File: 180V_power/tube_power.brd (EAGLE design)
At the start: 55 x 30 mm, 28 parts, among them IC1 NE555D, Q1 IRF740S, U1 TLV1117-5SOT-223, U2 2N7002

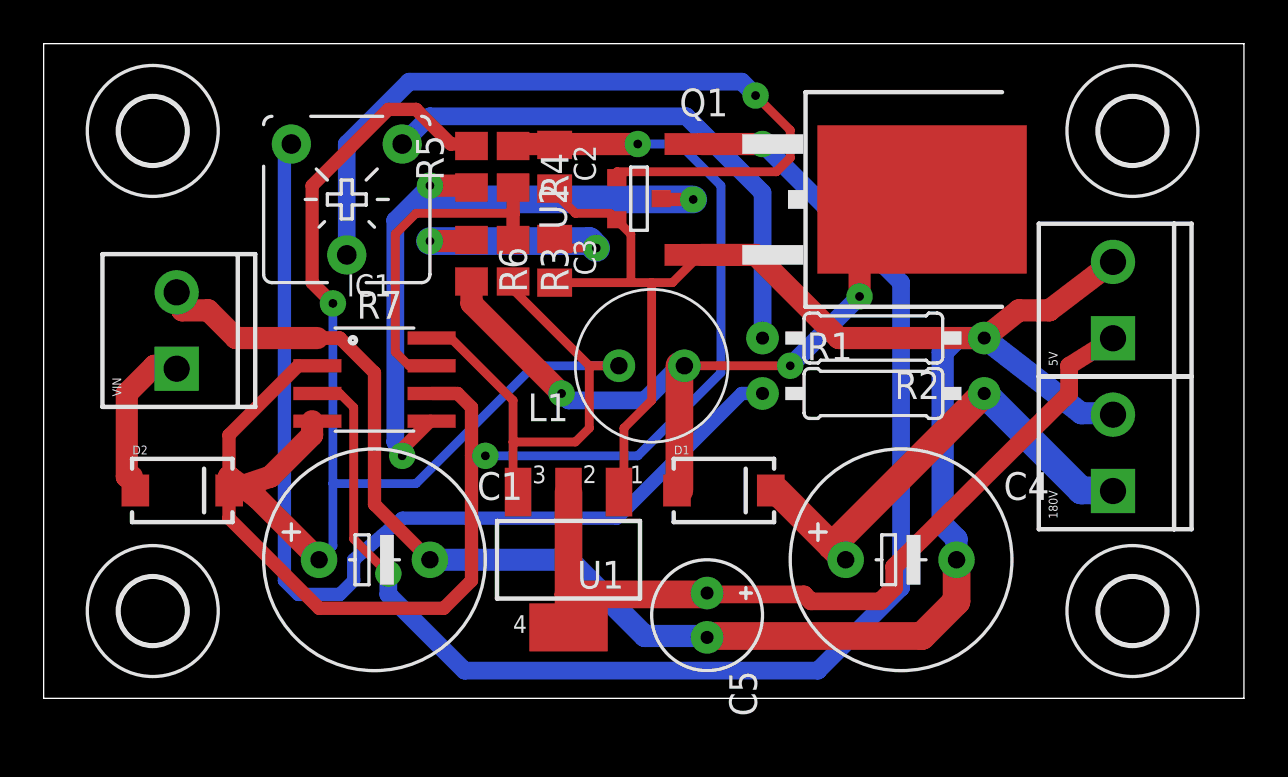
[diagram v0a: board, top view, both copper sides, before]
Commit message: new 180V board design
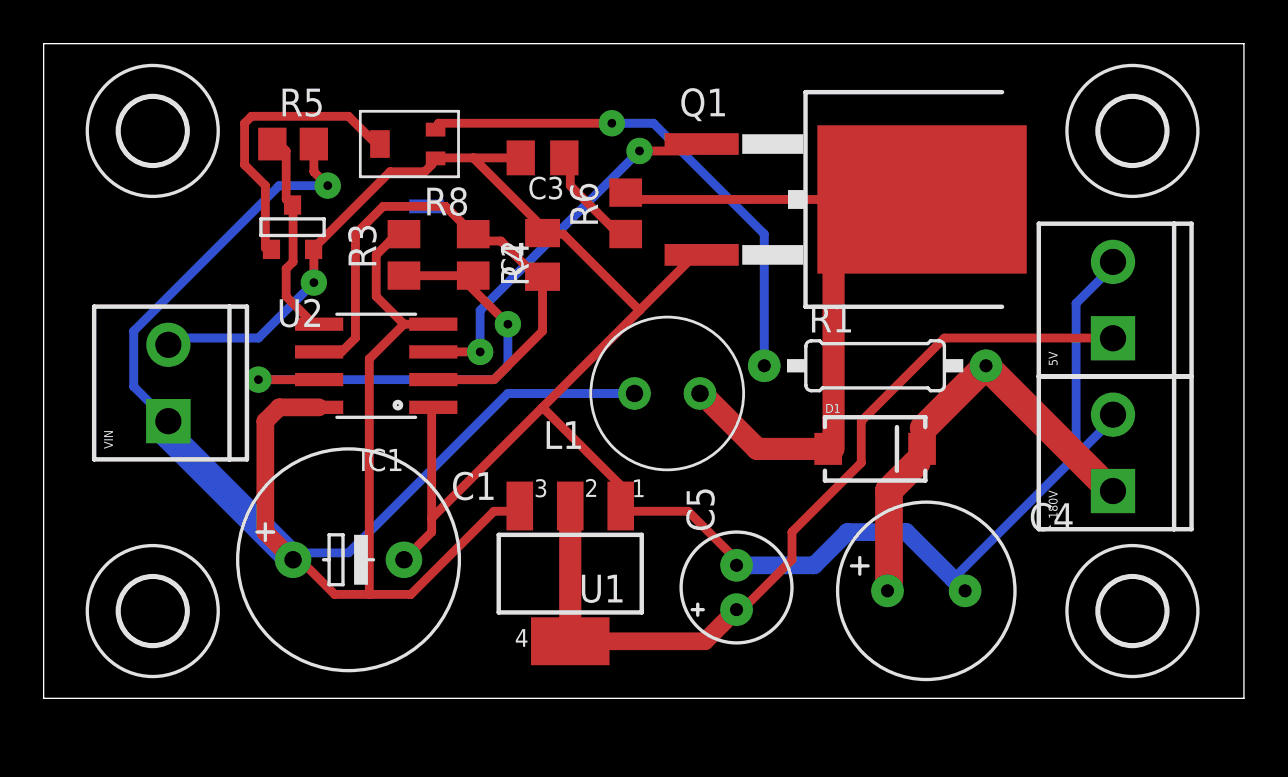
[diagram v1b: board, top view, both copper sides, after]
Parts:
- removed D2: (no value), iStivi - RCLD:SMA-DIODE
- removed R2: 470R, iStivi - RCLD:0207/10
- removed R7: 1K, iStivi - RCLD:CA6V
- added R8: (no value), iStivi - RCLD:TRIM-EVM2N
- C4: device iStivi - RCLD:E5-10,5 -> iStivi - RCLD:E3,5-8
- moved U2 15.9 mm to (11.4, 21.6), turned to 180 degrees
- moved R5 8.24 mm to (11.4, 25.4), turned to 0 degrees
- moved R6 7.39 mm to (26.7, 22.2), turned to 90 degrees
- moved D1 7.19 mm to (38.1, 11.4)
- moved R3 5.01 mm to (16.5, 20.3), turned to 90 degrees
- moved C3 4.75 mm to (22.9, 24.8), turned to 180 degrees
- moved R4 4.43 mm to (19.7, 20.3)
- moved C2 4.08 mm to (22.9, 20.3), turned to 90 degrees
- moved VIN 2.43 mm to (5.71, 12.7)
- moved C5 1.85 mm to (31.8, 5.08), turned to 90 degrees
- moved C4 1.83 mm to (40.4, 4.93)
- moved L1 1.46 mm to (28.6, 14.0)
- moved R1 1.27 mm to (38.1, 15.2)
- moved C1 1.19 mm to (14.0, 6.35)
- moved IC1 0.64 mm to (15.2, 15.2), turned to 90 degrees
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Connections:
- removed net R2: R2.2, R7.A
- removed net VAR: R7.S, U2.1
- net GND: now also R8.P$1; no longer R2.1
- net N$1: now also R8.P$2, U2.1; no longer D2.A, VIN.1
- net R1: now also R8.P$3; no longer R7.E
- net VCC: now also VIN.1; no longer D2.C
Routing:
- net OUT: track 63.4 -> 17.4 mm
- net THR: track 64.6 -> 25.8 mm, vias 2 -> 0
- net VAR: track 37.2 -> 0.00 mm, vias 1 -> 0
- net R2: track 25.2 -> 0.00 mm
- net R1: track 46.6 -> 23.4 mm, vias 0 -> 1
- net CON: track 31.2 -> 9.74 mm, vias 3 -> 0
- net GND: track 113.8 -> 101.4 mm, vias 0 -> 1
- net VCC: track 77.0 -> 88.4 mm
- net DIS: track 15.5 -> 23.3 mm, vias 0 -> 2
- net R6: track 11.8 -> 5.18 mm, vias 2 -> 0
- net N$1: track 7.57 -> 13.3 mm
- net 180V: track 22.5 -> 20.5 mm
- net L1: track 34.3 -> 32.5 mm, vias 3 -> 0
- net 5V: track 37.5 -> 38.7 mm
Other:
- board text added: "1"
- board text added: "2"
- board text added: "3"
- board text added: "4"
- board text added: "TUBE POWER SUPPLY"
- board text removed: "10uF"
- board text removed: "330uF"
- board text removed: "9-12V"
- board text removed: "C4"
- board text removed: "IRF740"
- board text removed: "L1"
- board text removed: "NIXIE POWER SUPPLY"
- board text removed: "R1"
- board text removed: "R2"
- board text removed: "TLV1117"
- board text removed: "VR1"

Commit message: added diode and resistor to 180V power
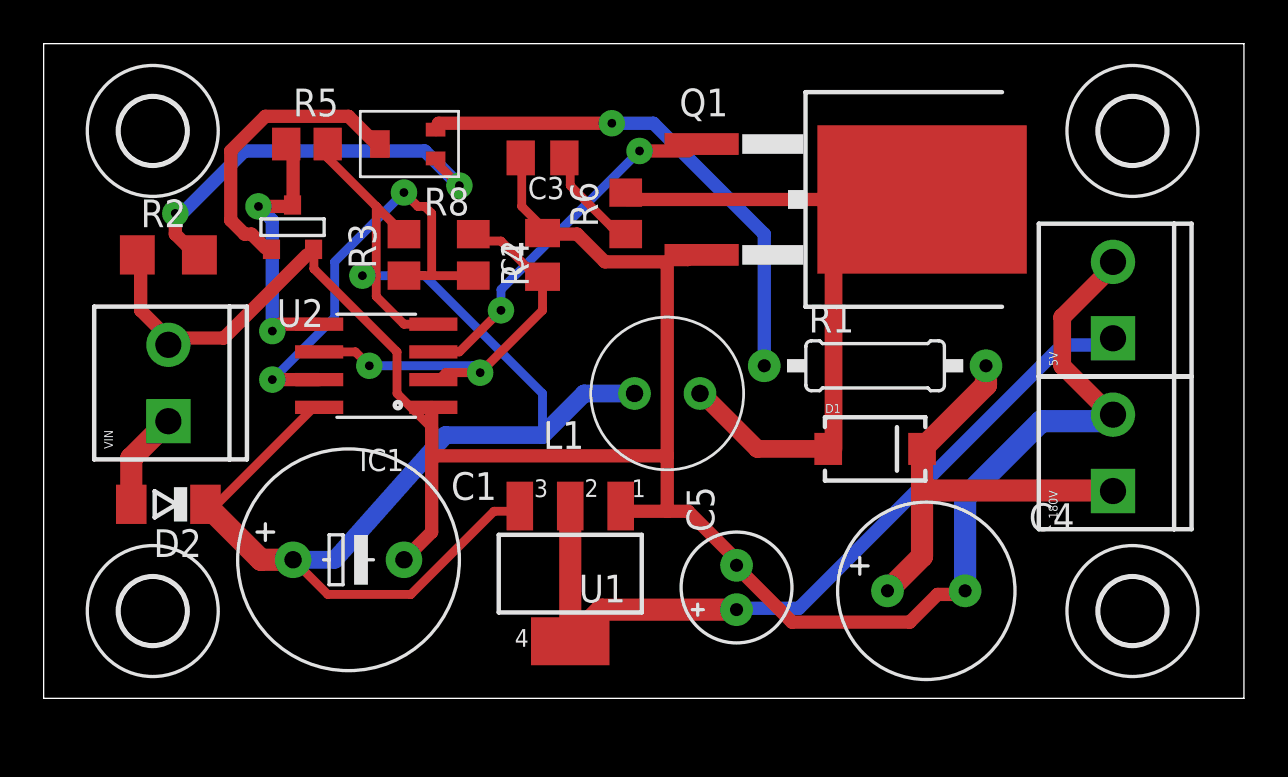
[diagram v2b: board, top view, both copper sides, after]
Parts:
- added D2: (no value), iStivi - RCLD:SOD80C
- added R2: (no value), iStivi - RCLD:R1206
- C2: value 2n2 -> 4n7
- L1: value 100uH -> 180uH
- R4: value 10K -> 3K3
- R8: value (none) -> 5K
- moved R5 0.63 mm to (12.1, 25.4)
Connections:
- new net N$2: D2.A, VIN.1
- new net N$3: R2.2, R8.P$1
- net GND: now also R2.1; no longer R8.P$1
- net VCC: now also D2.C; no longer VIN.1
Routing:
- net N$3: track 0.00 -> 19.0 mm, vias 0 -> 2
- net VCC: track 88.4 -> 69.7 mm
- net THR: track 25.8 -> 19.9 mm, vias 0 -> 2
- net GND: track 101.4 -> 107.2 mm, vias 1 -> 0
- net N$2: track 0.00 -> 4.51 mm
- net CON: track 9.74 -> 12.9 mm, vias 0 -> 2
- net DIS: track 23.3 -> 20.9 mm
- net 5V: track 38.7 -> 36.9 mm
- net OUT: track 17.4 -> 16.8 mm
